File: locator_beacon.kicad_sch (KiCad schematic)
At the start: 8 parts, among them J1 Conn_01x02, J3 Conn_01x01, J4 OSHW logo, J5 Conn_01x02, J6 Conn_01x01, J7 Conn_01x02, U13 Pico

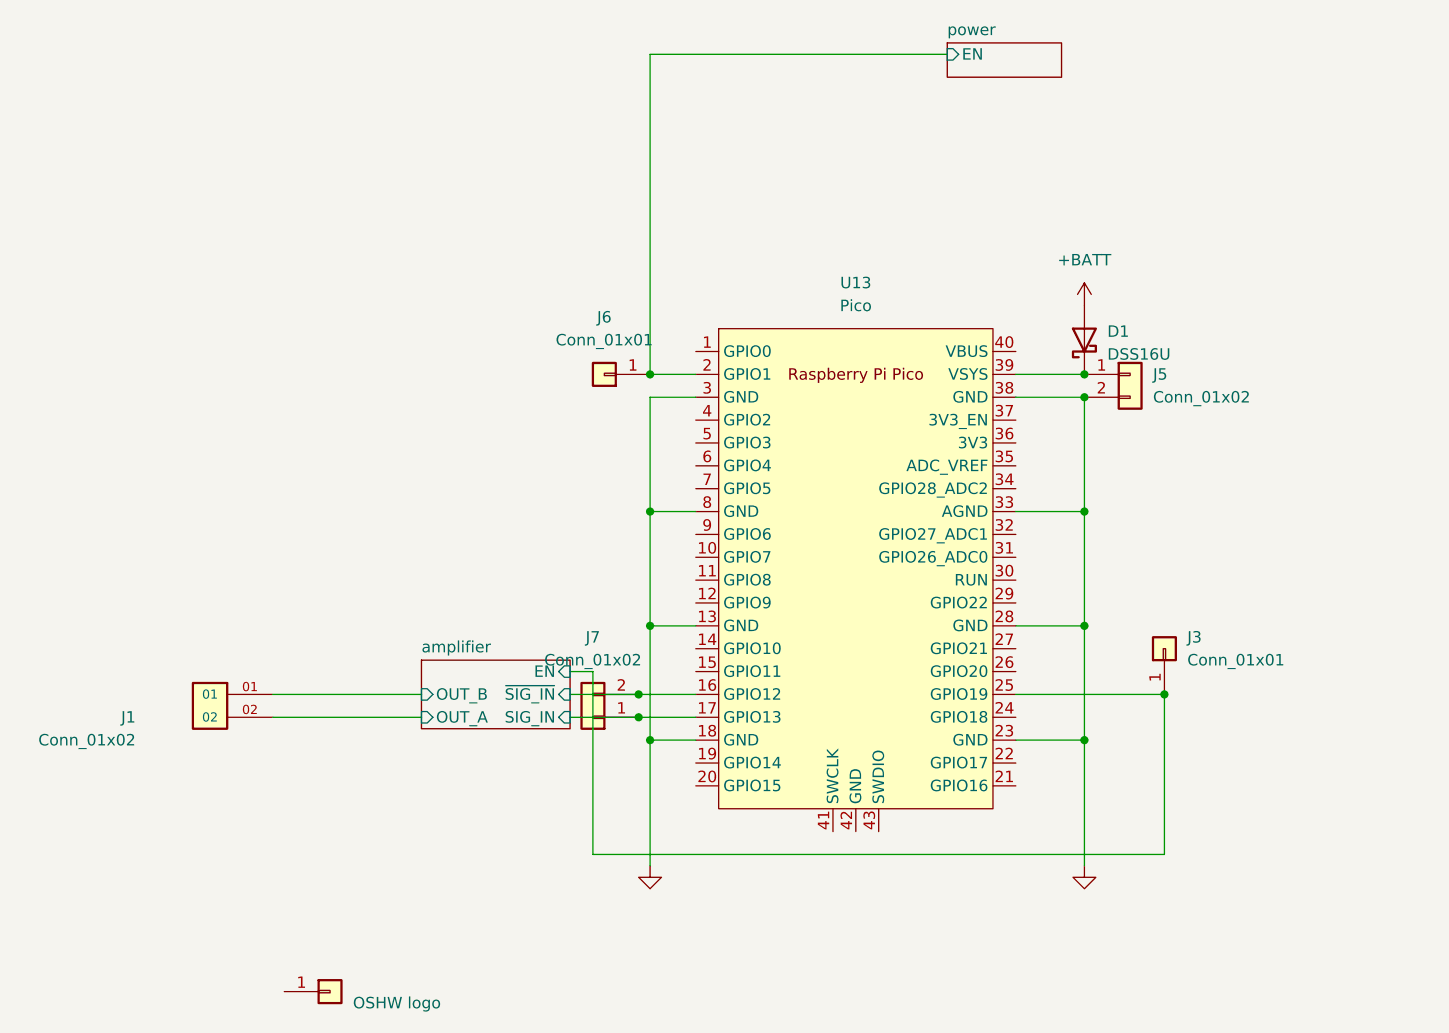
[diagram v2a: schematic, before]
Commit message: Separate +12 and boost
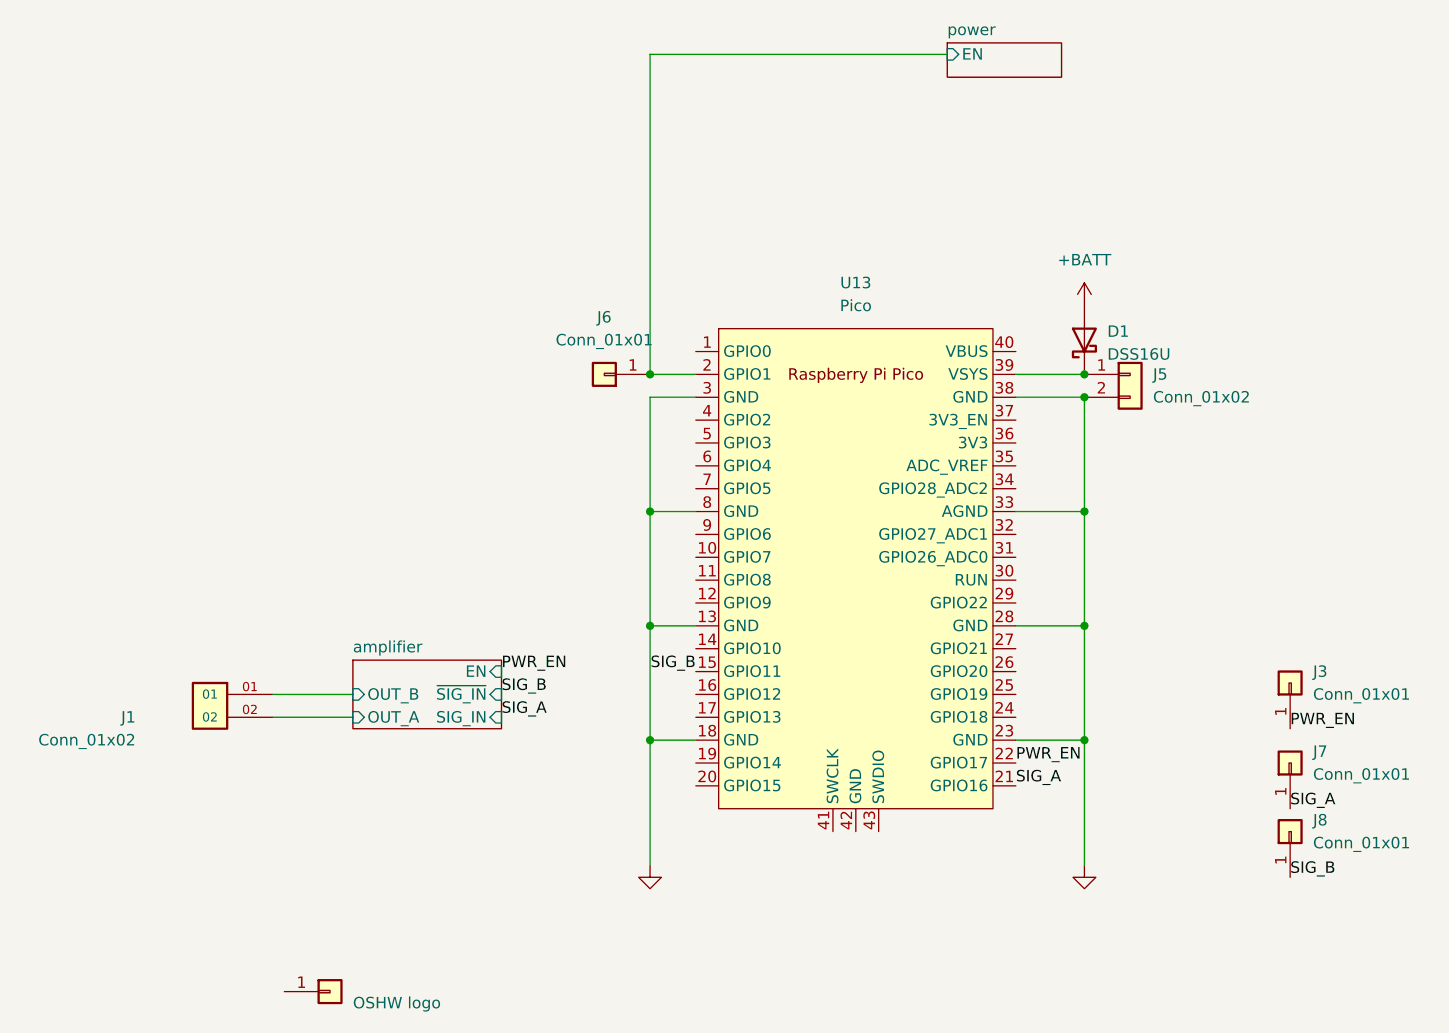
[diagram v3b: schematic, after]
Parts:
- removed J7: Conn_01x02, Connector_PinHeader_2.54mm:PinHeader_1x02_P2.54mm_Vertical, symbol Connector_Generic:Conn_01x02
- added J7, J8: Conn_01x01, Connector_PinHeader_2.54mm:PinHeader_1x01_P2.54mm_Vertical, symbol Connector_Generic:Conn_01x01
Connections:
- net SIG_B: now reaches U13.15 (GPIO11)
- net SIG_B: now also J8.1 (Pin_1)
- net SIG_A: now reaches U13.21 (GPIO16)
- net SIG_A: now also J7.1 (Pin_1)
- net PWR_EN: now reaches U13.22 (GPIO17)
- net PWR_EN: now also J3.1 (Pin_1)
- net amplifier/EN: no longer names the net of U13.25 (GPIO19)
- net amplifier/EN: no longer J3.1 (Pin_1)
- net amplifier/SIG_IN: no longer names the net of U13.17 (GPIO13)
- net amplifier/~{SIG_IN}: no longer names the net of U13.16 (GPIO12)
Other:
- moved on the sheet: J3
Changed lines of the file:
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@@
   (junction (at 123.19 124.46) (diameter 0) (color 0 0 0 0)
   )
-  (junction (at 73.66 121.92) (diameter 0) (color 0 0 0 0)
-  )
   (junction (at 74.93 124.46) (diameter 0) (color 0 0 0 0)
   )
@@
   (junction (at 123.19 86.36) (diameter 0) (color 0 0 0 0)
   )
-  (junction (at 132.08 119.38) (diameter 0) (color 0 0 0 0)
-  )
-  (junction (at 73.66 119.38) (diameter 0) (color 0 0 0 0)
-  )
   (junction (at 123.19 83.82) (diameter 0) (color 0 0 0 0)
   )
@@
   (junction (at 74.93 83.82) (diameter 0) (color 0 0 0 0)
   )
-  (wire (pts (xy 73.66 121.92) (xy 80.01 121.92))
-    (stroke (width 0) (type default))
-  )
   (wire (pts (xy 123.19 124.46) (xy 123.19 111.76))
     (stroke (width 0) (type default))
   )
-  (wire (pts (xy 115.57 119.38) (xy 132.08 119.38))
-    (stroke (width 0) (type default))
-  )
   (wire (pts (xy 80.01 83.82) (xy 74.93 83.82))
     (stroke (width 0) (type default))
@@
     (stroke (width 0) (type default))
   )
-  (wire (pts (xy 66.04 121.92) (xy 73.66 121.92))
-    (stroke (width 0) (type default))
-  )
   (wire (pts (xy 74.93 99.06) (xy 74.93 86.36))
     (stroke (width 0) (type default))
@@
     (stroke (width 0) (type default))
   )
-  (wire (pts (xy 66.04 119.38) (xy 73.66 119.38))
-    (stroke (width 0) (type default))
-  )
   (wire (pts (xy 74.93 48.26) (xy 107.95 48.26))
     (stroke (width 0) (type default))
@@
     (stroke (width 0) (type default))
   )
-  (wire (pts (xy 33.02 121.92) (xy 49.53 121.92))
+  (wire (pts (xy 33.02 121.92) (xy 41.91 121.92))
     (stroke (width 0) (type default))
   )
@@
     (stroke (width 0) (type default))
   )
-  (wire (pts (xy 132.08 119.38) (xy 132.08 137.16))
-    (stroke (width 0) (type default))
-  )
   (wire (pts (xy 74.93 138.43) (xy 74.93 124.46))
     (stroke (width 0) (type default))
   )
-  (wire (pts (xy 33.02 119.38) (xy 49.53 119.38))
-    (stroke (width 0) (type default))
-  )
-  (wire (pts (xy 73.66 119.38) (xy 80.01 119.38))
+  (wire (pts (xy 33.02 119.38) (xy 41.91 119.38))
     (stroke (width 0) (type default))
   )
@@
     (stroke (width 0) (type default))
   )
-  (wire (pts (xy 68.58 116.84) (xy 66.04 116.84))
-    (stroke (width 0) (type default))
-  )
   (wire (pts (xy 115.57 111.76) (xy 123.19 111.76))
     (stroke (width 0) (type default))
   )
-  (wire (pts (xy 132.08 137.16) (xy 68.58 137.16))
-    (stroke (width 0) (type default))
-  )
   (wire (pts (xy 115.57 83.82) (xy 123.19 83.82))
     (stroke (width 0) (type default))
@@
     (stroke (width 0) (type default))
   )
-  (wire (pts (xy 68.58 137.16) (xy 68.58 116.84))
-    (stroke (width 0) (type default))
-  )
   (wire (pts (xy 115.57 124.46) (xy 123.19 124.46))
     (stroke (width 0) (type default))
   )
-  (symbol (lib_id "Connector_Generic:Conn_01x02") (at 68.58 121.92 180) (unit 1)
-    (in_bom yes) (on_board yes) (dnp no) (fields_autoplaced)
-    (property "Reference" "J7" (at 68.58 113.03 0)
-      (effects (font (size 1.27 1.27)))
-    )
-    (property "Value" "Conn_01x02" (at 68.58 115.57 0)
-      (effects (font (size 1.27 1.27)))
-    )
-    (property "Footprint" "Connector_PinHeader_2.54mm:PinHeader_1x02_P2.54mm_Vertical" (at 68.58 121.92 0)
-      (effects (font (size 1.27 1.27)) hide)
-    )
-    (property "Datasheet" "~" (at 68.58 121.92 0)
-      (effects (font (size 1.27 1.27)) hide)
-    )
-    (pin "1")
-    (pin "2")
-    (instances
-      (project "locator_beacon"
-        (path "/2e37f9ca-1f81-48a3-bbbb-9eab5c177622"
-          (reference "J7") (unit 1)
-        )
-      )
-    )
+  (label "SIG_A" (at 146.05 132.08 0) (fields_autoplaced)
+    (effects (font (size 1.27 1.27)) (justify left bottom))
+  )
+  (label "SIG_B" (at 146.05 139.7 0) (fields_autoplaced)
+    (effects (font (size 1.27 1.27)) (justify left bottom))
+  )
+  (label "SIG_B" (at 80.01 116.84 180) (fields_autoplaced)
+    (effects (font (size 1.27 1.27)) (justify right bottom))
+  )
+  (label "SIG_A" (at 115.57 129.54 0) (fields_autoplaced)
+    (effects (font (size 1.27 1.27)) (justify left bottom))
+  )
+  (label "SIG_B" (at 58.42 119.38 0) (fields_autoplaced)
+    (effects (font (size 1.27 1.27)) (justify left bottom))
+  )
+  (label "SIG_A" (at 58.42 121.92 0) (fields_autoplaced)
+    (effects (font (size 1.27 1.27)) (justify left bottom))
+  )
+  (label "PWR_EN" (at 58.42 116.84 0) (fields_autoplaced)
+    (effects (font (size 1.27 1.27)) (justify left bottom))
+  )
+  (label "PWR_EN" (at 115.57 127 0) (fields_autoplaced)
+    (effects (font (size 1.27 1.27)) (justify left bottom))
+  )
+  (label "PWR_EN" (at 146.05 123.19 0) (fields_autoplaced)
+    (effects (font (size 1.27 1.27)) (justify left bottom))
   )
   (symbol (lib_id "custom_symbols:TSM-102-01-L-SH") (at 20.32 121.92 0) (mirror y) (unit 1)
@@
         (path "/2e37f9ca-1f81-48a3-bbbb-9eab5c177622"
           (reference "#PWR08") (unit 1)
+        )
+      )
+    )
+  )
+  (symbol (lib_id "Connector_Generic:Conn_01x01") (at 146.05 134.62 90) (unit 1)
+    (in_bom yes) (on_board yes) (dnp no) (fields_autoplaced)
+    (property "Reference" "J8" (at 148.59 133.35 90)
+      (effects (font (size 1.27 1.27)) (justify right))
+    )
+    (property "Value" "Conn_01x01" (at 148.59 135.89 90)
+      (effects (font (size 1.27 1.27)) (justify right))
+    )
+    (property "Footprint" "Connector_PinHeader_2.54mm:PinHeader_1x01_P2.54mm_Vertical" (at 146.05 134.62 0)
+      (effects (font (size 1.27 1.27)) hide)
+    )
+    (property "Datasheet" "~" (at 146.05 134.62 0)
+      (effects (font (size 1.27 1.27)) hide)
+    )
+    (pin "1")
+    (instances
+      (project "locator_beacon"
+        (path "/2e37f9ca-1f81-48a3-bbbb-9eab5c177622"
+          (reference "J8") (unit 1)
         )
       )
@@
     )
   )
-  (symbol (lib_id "Connector_Generic:Conn_01x01") (at 132.08 114.3 90) (unit 1)
-    (in_bom yes) (on_board yes) (dnp no) (fields_autoplaced)
-    (property "Reference" "J3" (at 134.62 113.03 90)
-      (effects (font (size 1.27 1.27)) (justify right))
-    )
-    (property "Value" "Conn_01x01" (at 134.62 115.57 90)
-      (effects (font (size 1.27 1.27)) (justify right))
-    )
-    (property "Footprint" "Connector_PinHeader_2.54mm:PinHeader_1x01_P2.54mm_Vertical" (at 132.08 114.3 0)
-      (effects (font (size 1.27 1.27)) hide)
-    )
-    (property "Datasheet" "~" (at 132.08 114.3 0)
+  (symbol (lib_id "Connector_Generic:Conn_01x01") (at 146.05 118.11 90) (unit 1)
+    (in_bom yes) (on_board yes) (dnp no) (fields_autoplaced)
+    (property "Reference" "J3" (at 148.59 116.84 90)
+      (effects (font (size 1.27 1.27)) (justify right))
+    )
+    (property "Value" "Conn_01x01" (at 148.59 119.38 90)
+      (effects (font (size 1.27 1.27)) (justify right))
+    )
+    (property "Footprint" "Connector_PinHeader_2.54mm:PinHeader_1x01_P2.54mm_Vertical" (at 146.05 118.11 0)
+      (effects (font (size 1.27 1.27)) hide)
+    )
+    (property "Datasheet" "~" (at 146.05 118.11 0)
       (effects (font (size 1.27 1.27)) hide)
     )
@@
         (path "/2e37f9ca-1f81-48a3-bbbb-9eab5c177622"
           (reference "J3") (unit 1)
+        )
+      )
+    )
+  )
+  (symbol (lib_id "Connector_Generic:Conn_01x01") (at 146.05 127 90) (unit 1)
+    (in_bom yes) (on_board yes) (dnp no) (fields_autoplaced)
+    (property "Reference" "J7" (at 148.59 125.73 90)
+      (effects (font (size 1.27 1.27)) (justify right))
+    )
+    (property "Value" "Conn_01x01" (at 148.59 128.27 90)
+      (effects (font (size 1.27 1.27)) (justify right))
+    )
+    (property "Footprint" "Connector_PinHeader_2.54mm:PinHeader_1x01_P2.54mm_Vertical" (at 146.05 127 0)
+      (effects (font (size 1.27 1.27)) hide)
+    )
+    (property "Datasheet" "~" (at 146.05 127 0)
+      (effects (font (size 1.27 1.27)) hide)
+    )
+    (pin "1")
+    (instances
+      (project "locator_beacon"
+        (path "/2e37f9ca-1f81-48a3-bbbb-9eab5c177622"
+          (reference "J7") (unit 1)
         )
       )
@@
     )
   )
-  (sheet (at 49.53 115.57) (size 16.51 7.62) (fields_autoplaced)
+  (sheet (at 41.91 115.57) (size 16.51 7.62) (fields_autoplaced)
     (stroke (width 0.1524) (type solid))
     (fill (color 0 0 0 0.0000))
-    (property "Sheetname" "amplifier" (at 49.53 114.8584 0)
+    (property "Sheetname" "amplifier" (at 41.91 114.8584 0)
       (effects (font (size 1.27 1.27)) (justify left bottom))
     )
-    (property "Sheetfile" "amplifier.kicad_sch" (at 49.53 123.7746 0)
+    (property "Sheetfile" "amplifier.kicad_sch" (at 41.91 123.7746 0)
       (effects (font (size 1.27 1.27)) (justify left top) hide)
     )
-    (pin "SIG_IN" input (at 66.04 121.92 0)
-      (effects (font (size 1.27 1.27)) (justify right))
-    )
-    (pin "OUT_A" input (at 49.53 121.92 180)
-      (effects (font (size 1.27 1.27)) (justify left))
-    )
-    (pin "OUT_B" input (at 49.53 119.38 180)
-      (effects (font (size 1.27 1.27)) (justify left))
-    )
-    (pin "~{SIG_IN}" input (at 66.04 119.38 0)
-      (effects (font (size 1.27 1.27)) (justify right))
-    )
-    (pin "EN" input (at 66.04 116.84 0)
-      (effects (font (size 1.27 1.27)) (justify right))
-    )
+    (pin "SIG_IN" input (at 58.42 121.92 0)
+      (effects (font (size 1.27 1.27)) (justify right))
+    )
+    (pin "OUT_A" input (at 41.91 121.92 180)
+      (effects (font (size 1.27 1.27)) (justify left))
+    )
+    (pin "OUT_B" input (at 41.91 119.38 180)
+      (effects (font (size 1.27 1.27)) (justify left))
+    )
+    (pin "~{SIG_IN}" input (at 58.42 119.38 0)
+      (effects (font (size 1.27 1.27)) (justify right))
+    )
+    (pin "EN" input (at 58.42 116.84 0)
+      (effects (font (size 1.27 1.27)) (justify right))
+    )
